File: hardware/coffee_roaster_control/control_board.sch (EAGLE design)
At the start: 2 parts, among them SW1 EC12E_SW

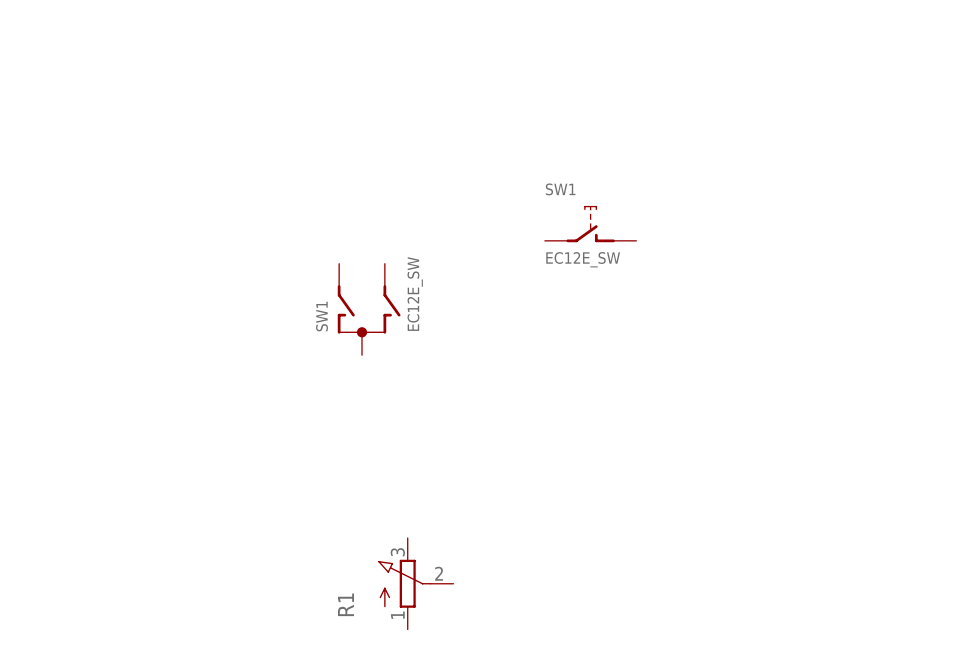
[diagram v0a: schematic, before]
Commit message: added irlb8721
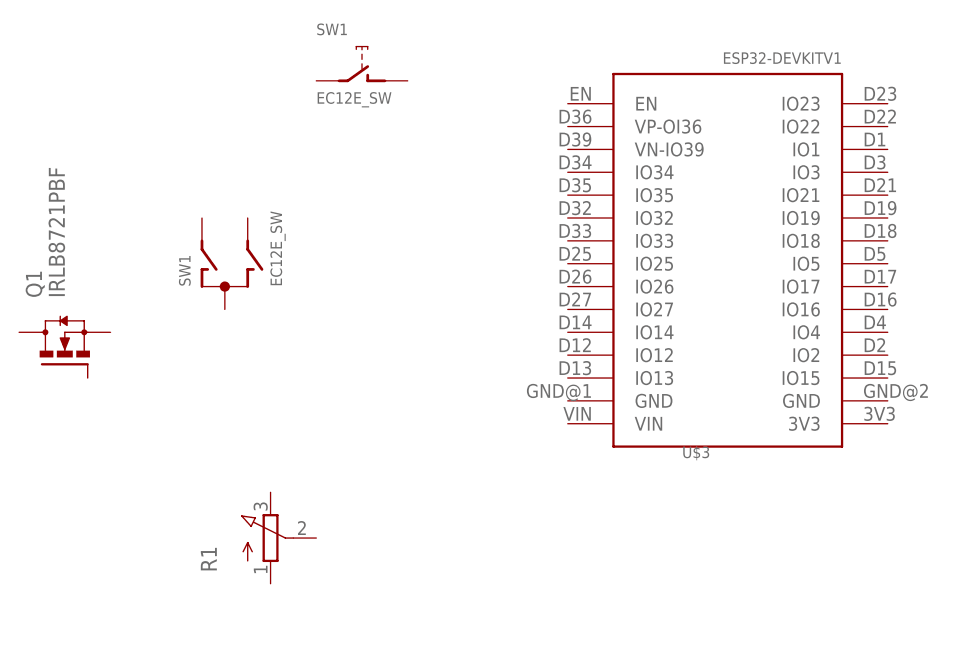
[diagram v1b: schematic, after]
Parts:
- added Q1, U$1, U$2: IRLB8721PBF, drue_custom:IRLB8721PBF
- added U$3: ESP32DEVKITV1, ESP32-DEVKITV1:ESP32DEVKITV1
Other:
- moved on the sheet: R1, SW1
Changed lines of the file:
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@@
 <setting verticaltext="up"/>
 </settings>
-<grid distance="0.1" unitdist="inch" unit="inch" style="lines" multiple="1" display="yes" altdistance="0.01" altunitdist="inch" altunit="inch"/>
+<grid distance="0.1" unitdist="inch" unit="inch" style="lines" multiple="1" display="no" altdistance="0.01" altunitdist="inch" altunit="inch"/>
 <layers>
 <layer number="1" name="Top" color="4" fill="1" visible="no" active="no"/>
@@
 <part name="SW1" library="switch-alps" library_urn="urn:adsk.eagle:library:373" deviceset="EC12E_SW" device="" package3d_urn="urn:adsk.eagle:package:27083/1"/>
 <part name="R1" library="pot" library_urn="urn:adsk.eagle:library:331" deviceset="3RP/1610N" device="" package3d_urn="urn:adsk.eagle:package:22726/1"/>
+<part name="U$1" library="drue_custom" deviceset="IRLB8721PBF" device="" package3d_urn="urn:adsk.eagle:package:29484/4"/>
+<part name="U$2" library="drue_custom" deviceset="IRLB8721PBF" device="" package3d_urn="urn:adsk.eagle:package:29484/4"/>
+<part name="U$3" library="ESP32-DEVKITV1" deviceset="ESP32DEVKITV1" device=""/>
+<part name="Q1" library="drue_custom" deviceset="IRLB8721PBF" device="" package3d_urn="urn:adsk.eagle:package:29484/4"/>
 </parts>
 <sheets>
@@
 </plain>
 <instances>
-<instance part="SW1" gate="G$1" x="20.32" y="33.02" smashed="yes">
-<attribute name="PART" x="16.51" y="33.02" size="1.27" layer="95" rot="R90"/>
-<attribute name="VALUE" x="26.67" y="33.02" size="1.27" layer="96" rot="R90"/>
+<instance part="SW1" gate="G$1" x="5.08" y="38.1" smashed="yes">
+<attribute name="PART" x="1.27" y="38.1" size="1.27" layer="95" rot="R90"/>
+<attribute name="VALUE" x="11.43" y="38.1" size="1.27" layer="96" rot="R90"/>
 </instance>
-<instance part="SW1" gate="G$2" x="45.72" y="43.18" smashed="yes">
-<attribute name="PART" x="40.64" y="48.26" size="1.27" layer="95"/>
-<attribute name="VALUE" x="40.64" y="40.64" size="1.27" layer="96"/>
+<instance part="SW1" gate="G$2" x="20.32" y="60.96" smashed="yes">
+<attribute name="PART" x="15.24" y="66.04" size="1.27" layer="95"/>
+<attribute name="VALUE" x="15.24" y="58.42" size="1.27" layer="96"/>
 </instance>
-<instance part="R1" gate="G$1" x="25.4" y="5.08" smashed="yes">
-<attribute name="NAME" x="19.431" y="1.27" size="1.778" layer="95" rot="R90"/>
-<attribute name="VALUE" x="21.59" y="1.27" size="1.778" layer="96" rot="R90"/>
+<instance part="R1" gate="G$1" x="10.16" y="10.16" smashed="yes">
+<attribute name="NAME" x="4.191" y="6.35" size="1.778" layer="95" rot="R90"/>
+<attribute name="VALUE" x="6.35" y="6.35" size="1.778" layer="96" rot="R90"/>
+</instance>
+<instance part="U$3" gate="G$1" x="60.96" y="45.72" smashed="yes" rot="R90">
+<attribute name="NAME" x="55.88" y="19.05" size="1.27" layer="95"/>
+</instance>
+<instance part="Q1" gate="G$1" x="-12.7" y="30.48" smashed="yes" rot="R90">
+<attribute name="NAME" x="-15.24" y="36.83" size="1.778" layer="95" rot="R90"/>
+<attribute name="VALUE" x="-12.7" y="36.83" size="1.778" layer="96" rot="R90"/>
 </instance>
 </instances>
